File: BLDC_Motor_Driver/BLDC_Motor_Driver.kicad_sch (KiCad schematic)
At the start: 45 parts, among them J101 Conn_01x08, J102 395221002, J103 USB4105-GF-A, J104 Conn_01x05, J105 Conn_01x05, J106 Conn_01x04, J107 395221005, J108 395221003, J109 Conn_02x12_Counter_Clockwise, J110 395221005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

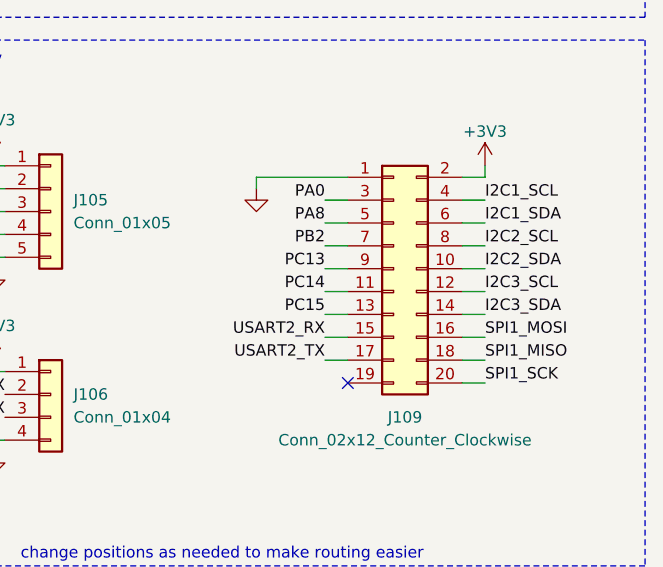
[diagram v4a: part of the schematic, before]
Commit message: finsihed first draft. DRC errors remaining
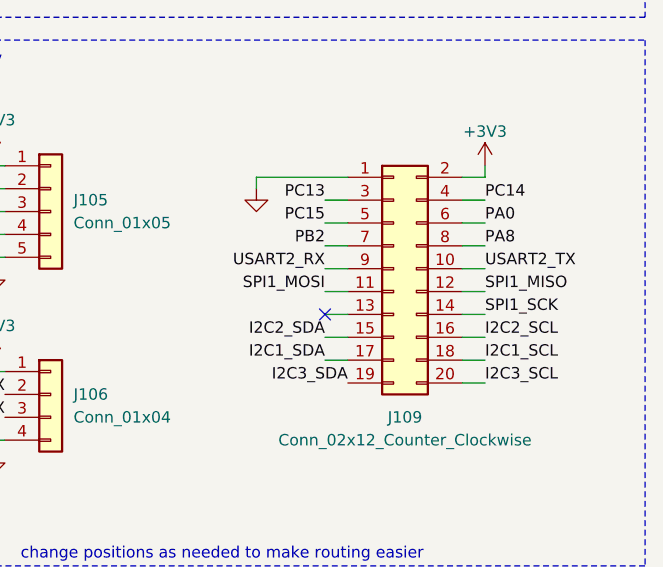
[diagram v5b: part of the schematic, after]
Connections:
- net I2C1_SCL: now also J109.18 (Pin_18); no longer J109.4 (Pin_4)
- net I2C1_SDA: now also J109.17 (Pin_17); no longer J109.6 (Pin_6)
- net I2C2_SCL: now also J109.16 (Pin_16); no longer J109.8 (Pin_8)
- net I2C2_SDA: now also J109.15 (Pin_15); no longer J109.10 (Pin_10)
- net I2C3_SCL: now also J109.20 (Pin_20); no longer J109.12 (Pin_12)
- net I2C3_SDA: now also J109.19 (Pin_19); no longer J109.14 (Pin_14)
- net PA0: now also J109.6 (Pin_6); no longer J109.3 (Pin_3)
- net PA8: now also J109.8 (Pin_8); no longer J109.5 (Pin_5)
- net PC13: now also J109.3 (Pin_3); no longer J109.9 (Pin_9)
- net PC14: now also J109.4 (Pin_4); no longer J109.11 (Pin_11)
- net PC15: now also J109.5 (Pin_5); no longer J109.13 (Pin_13)
- net SPI1_MISO: now also J109.12 (Pin_12); no longer J109.18 (Pin_18)
- net SPI1_MOSI: now also J109.11 (Pin_11); no longer J109.16 (Pin_16)
- net SPI1_SCK: now also J109.14 (Pin_14); no longer J109.20 (Pin_20)
- net USART2_RX: now also J109.9 (Pin_9); no longer J109.15 (Pin_15)
- net USART2_TX: now also J109.10 (Pin_10); no longer J109.17 (Pin_17)
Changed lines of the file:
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@@
 	)
 	(no_connect
-		(at 248.92 142.24)
+		(at 246.38 134.62)
 	)
 	(no_connect
@@
 	)
 	(label "USART2_RX"
-		(at 246.38 137.16 180)
+		(at 246.38 129.54 180)
 		(effects
 			(font
@@
 	)
 	(label "PC15"
-		(at 246.38 134.62 180)
+		(at 246.38 124.46 180)
 		(effects
 			(font
@@
 	)
 	(label "PC13"
-		(at 246.38 129.54 180)
+		(at 246.38 121.92 180)
 		(effects
 			(font
@@
 	)
 	(label "SPI1_SCK"
-		(at 264.16 142.24 0)
+		(at 264.16 134.62 0)
 		(effects
 			(font
@@
 	)
 	(label "SPI1_MOSI"
-		(at 264.16 137.16 0)
+		(at 246.38 132.08 180)
 		(effects
 			(font
 				(size 1.27 1.27)
 			)
-			(justify left bottom)
+			(justify right bottom)
 		)
 	)
@@
 	)
 	(label "PA8"
-		(at 246.38 124.46 180)
+		(at 264.16 127 0)
 		(effects
 			(font
 				(size 1.27 1.27)
 			)
-			(justify right bottom)
+			(justify left bottom)
 		)
 	)
@@
 	)
 	(label "I2C1_SCL"
-		(at 264.16 121.92 0)
+		(at 264.16 139.7 0)
 		(effects
 			(font
@@
 	)
 	(label "PC14"
-		(at 246.38 132.08 180)
+		(at 264.16 121.92 0)
 		(effects
 			(font
 				(size 1.27 1.27)
 			)
-			(justify right bottom)
+			(justify left bottom)
 		)
 	)
@@
 	)
 	(label "PA0"
-		(at 246.38 121.92 180)
+		(at 264.16 124.46 0)
 		(effects
 			(font
 				(size 1.27 1.27)
 			)
-			(justify right bottom)
+			(justify left bottom)
 		)
 	)
@@
 	)
 	(label "USART2_TX"
-		(at 246.38 139.7 180)
+		(at 264.16 129.54 0)
 		(effects
 			(font
 				(size 1.27 1.27)
 			)
-			(justify right bottom)
+			(justify left bottom)
 		)
 	)
 	(label "I2C3_SCL"
-		(at 264.16 132.08 0)
+		(at 264.16 142.24 0)
 		(effects
 			(font
@@
 	)
 	(label "I2C2_SCL"
-		(at 264.16 127 0)
+		(at 264.16 137.16 0)
 		(effects
 			(font
@@
 	)
 	(label "I2C1_SDA"
-		(at 264.16 124.46 0)
+		(at 246.38 139.7 180)
 		(effects
 			(font
 				(size 1.27 1.27)
 			)
-			(justify left bottom)
+			(justify right bottom)
 		)
 	)
@@
 	)
 	(label "I2C3_SDA"
-		(at 264.16 134.62 0)
+		(at 248.92 142.24 180)
 		(effects
 			(font
 				(size 1.27 1.27)
 			)
-			(justify left bottom)
+			(justify right bottom)
 		)
 	)
@@
 	)
 	(label "I2C2_SDA"
-		(at 264.16 129.54 0)
+		(at 246.38 137.16 180)
 		(effects
 			(font
 				(size 1.27 1.27)
 			)
-			(justify left bottom)
+			(justify right bottom)
 		)
 	)
@@
 	)
 	(label "SPI1_MISO"
-		(at 264.16 139.7 0)
+		(at 264.16 132.08 0)
 		(effects
 			(font
